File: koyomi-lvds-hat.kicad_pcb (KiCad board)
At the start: 2 copper layers, 65 x 56.5 mm, 27 parts, among them IC1 SN75LVDS83B, J1 RPi_GPIO, J2 20374-R30E-31, J3 aux_sig, J4 qwiic, J5 Conn_01x06, J6 Conn_01x06, J7 Conn_01x06, J8 i2c, U1 AP2114H-2.5

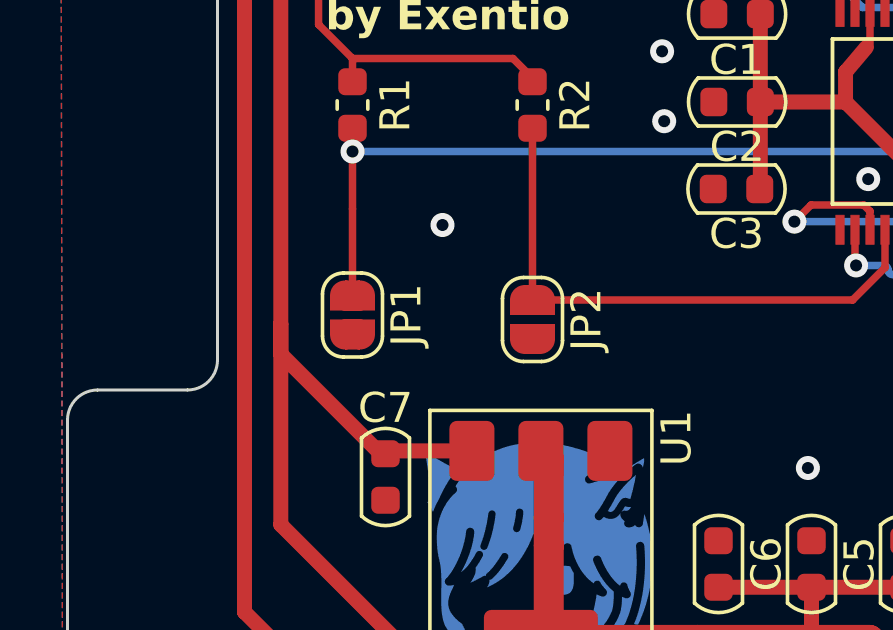
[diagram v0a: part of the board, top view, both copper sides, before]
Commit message: Added 3D models, labels fix
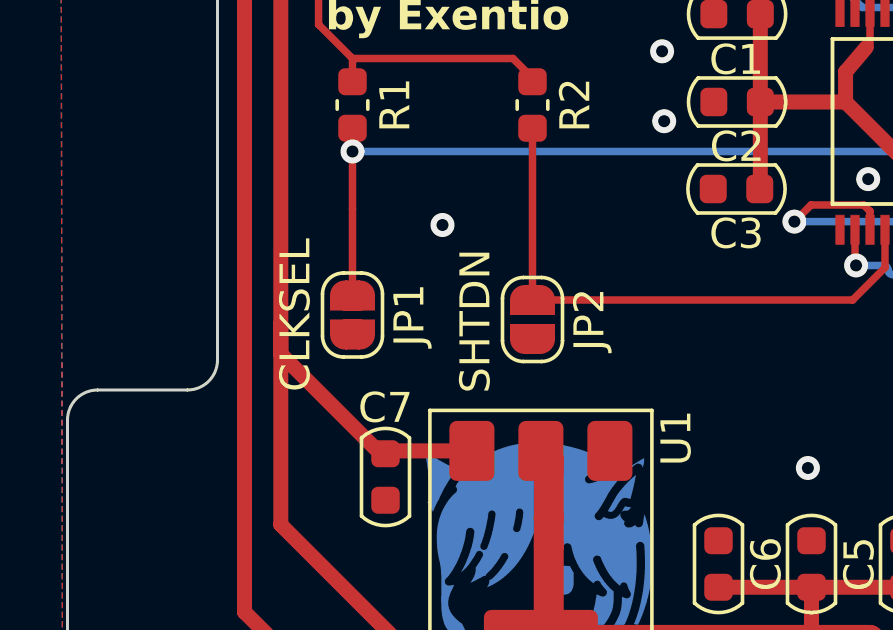
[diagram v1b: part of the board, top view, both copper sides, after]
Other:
- board text added: "CLKSEL"
- board text added: "SHTDN"
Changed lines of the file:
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@@
 		(tags "solder jumper open")
 		(property "Reference" "JP1"
-			(at 0 -1.8 90)
+			(at 0 -1.9 90)
 			(layer "F.SilkS")
 			(effects
@@
 			(at 0 1.9 90)
 			(layer "F.Fab")
+			(hide yes)
 			(effects
 				(font
@@
 			(pintype "passive")
 		)
+		(model "${KIPRJMOD}/lib/20374-R30E-31/20374-R30E-31.step"
+			(offset
+				(xyz 0 0 0)
+			)
+			(scale
+				(xyz 1 1 1)
+			)
+			(rotate
+				(xyz -90 0 180)
+			)
+		)
 	)
 	(footprint "Connector_PinSocket_2.54mm:PinSocket_1x05_P2.54mm_Vertical"
@@
 			(pintype "bidirectional")
 		)
+		(model "${KIPRJMOD}/lib/RPi_Hat_Template/Samtec_HLE-120-02-XXX-DV-BE-XX-XX.stp"
+			(offset
+				(xyz 0 0 0.1)
+			)
+			(scale
+				(xyz 1 1 1)
+			)
+			(rotate
+				(xyz -90 0 90)
+			)
+		)
 	)
 	(footprint "Connector_PinSocket_2.54mm:PinSocket_1x06_P2.54mm_Vertical"
@@
 		)
 		(property "Value" "SN75LVDS83B"
-			(at 0 0 0)
+			(at 0 0 180)
 			(layer "F.Fab")
 			(effects
@@
 		)
 		(property "Description" "\n5/0 Driver LVDS 56-BGA MICROSTAR JUNIOR (7.0x4.5)\n"
-			(at 123.5 50 0)
+			(at 123.5 50 180)
 			(layer "F.Fab")
 			(hide yes)
@@
 		)
 		(property "Availability" "Not in stock"
-			(at 0 0 0)
+			(at 0 0 180)
 			(layer "F.Fab")
 			(hide yes)
@@
 		)
 		(property "Check_prices" "https://www.snapeda.com/parts/SN75LVDS83B/Texas+Instruments/view-part/?ref=eda"
-			(at 0 0 0)
+			(at 0 0 180)
 			(layer "F.Fab")
 			(hide yes)
@@
 		)
 		(property "DIGIKEY" "296-24529-6-ND"
-			(at 0 0 0)
+			(at 0 0 180)
 			(layer "F.Fab")
 			(hide yes)
@@
 		)
 		(property "MF" "Texas Instruments"
-			(at 0 0 0)
+			(at 0 0 180)
 			(layer "F.Fab")
 			(hide yes)
@@
 		)
 		(property "MP" "SN75LVDS83B"
-			(at 0 0 0)
+			(at 0 0 180)
 			(layer "F.Fab")
 			(hide yes)
@@
 		)
 		(property "Package" "TFSOP-56 Texas Instruments"
-			(at 0 0 0)
+			(at 0 0 180)
 			(layer "F.Fab")
 			(hide yes)
@@
 		)
 		(property "Price" "None"
-			(at 0 0 0)
+			(at 0 0 180)
 			(layer "F.Fab")
 			(hide yes)
@@
 		)
 		(property "SnapEDA_Link" "https://www.snapeda.com/parts/SN75LVDS83B/Texas+Instruments/view-part/?ref=snap"
-			(at 0 0 0)
+			(at 0 0 180)
 			(layer "F.Fab")
 			(hide yes)
@@
 			(pintype "bidirectional")
 		)
+		(model "${KIPRJMOD}/lib/SN75LVDS83B/SN75LVDS83B.step"
+			(offset
+				(xyz 0 0 0)
+			)
+			(scale
+				(xyz 1 1 1)
+			)
+			(rotate
+				(xyz -90 0 90)
+			)
+		)
 	)
 	(footprint "Connector_PinHeader_2.54mm:PinHeader_1x06_P2.54mm_Vertical"
@@
 		(tags "solder jumper open")
 		(property "Reference" "JP2"
-			(at 0 -1.8 90)
+			(at 0 -1.9 90)
 			(layer "F.SilkS")
 			(effects
@@
 			(at 0 1.9 90)
 			(layer "F.Fab")
+			(hide yes)
 			(effects
 				(font
@@
 			(pintype "passive")
 		)
-		(model "${KICAD6_3DMODEL_DIR}/Connector_JST.3dshapes/JST_SH_SM04B-SRSS-TB_1x04-1MP_P1.00mm_Horizontal.wrl"
+		(model "${KIPRJMOD}/lib/JST_SH_SM04B-SRSS-TB_1x04-1MP_P1.00mm_Horizontal.STEP"
 			(offset
-				(xyz 0 0 0)
+				(xyz 0 1.35 -0.3)
 			)
 			(scale
@@
 			)
 			(rotate
-				(xyz 0 0 0)
+				(xyz -90 0 0)
 			)
 		)
@@
 		)
 	)
+	(gr_text "SHTDN"
+		(at 104.6 56.7 90)
+		(layer "F.SilkS")
+		(effects
+			(font
+				(size 1 1)
+				(thickness 0.15)
+			)
+		)
+	)
+	(gr_text "CLKSEL"
+		(at 98.6 56.5 90)
+		(layer "F.SilkS")
+		(effects
+			(font
+				(size 1 1)
+				(thickness 0.15)
+			)
+		)
+	)

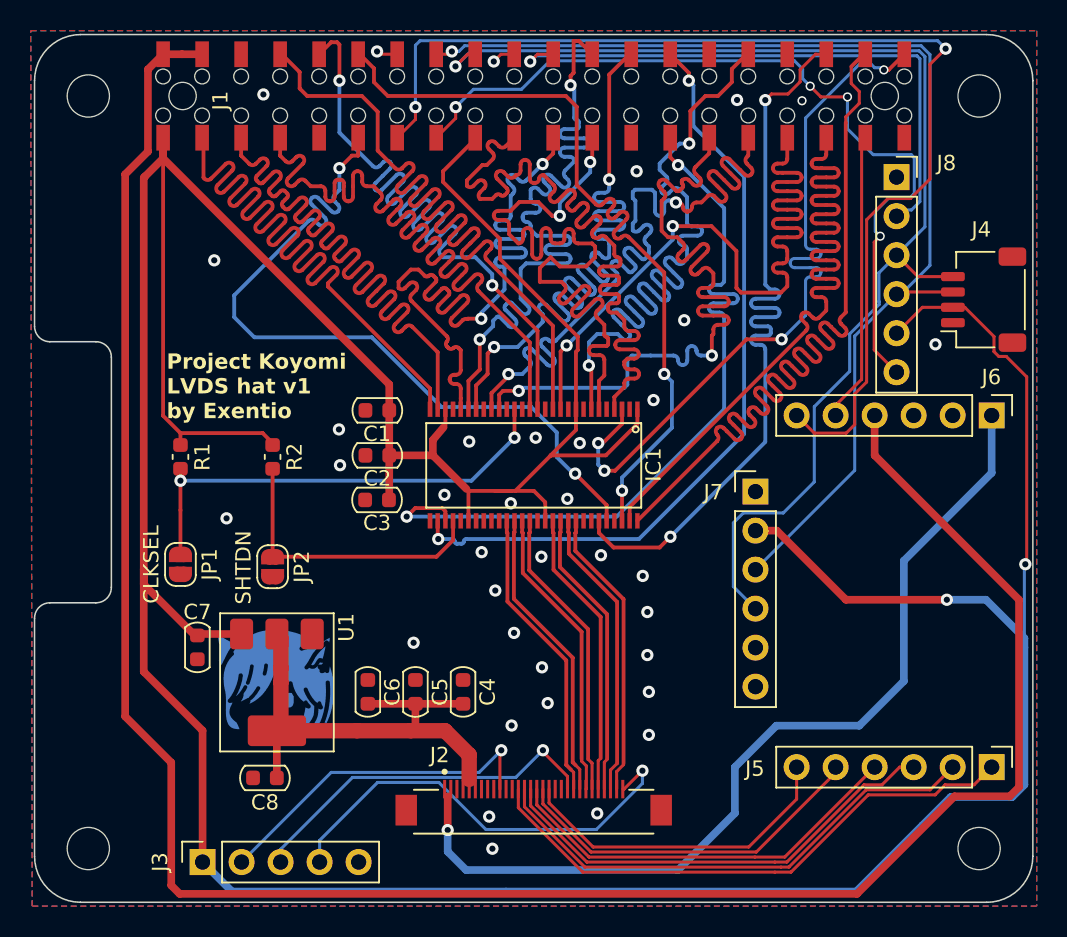
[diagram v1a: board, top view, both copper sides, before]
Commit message: v1.1 - fixed hat connector side, added series resistors
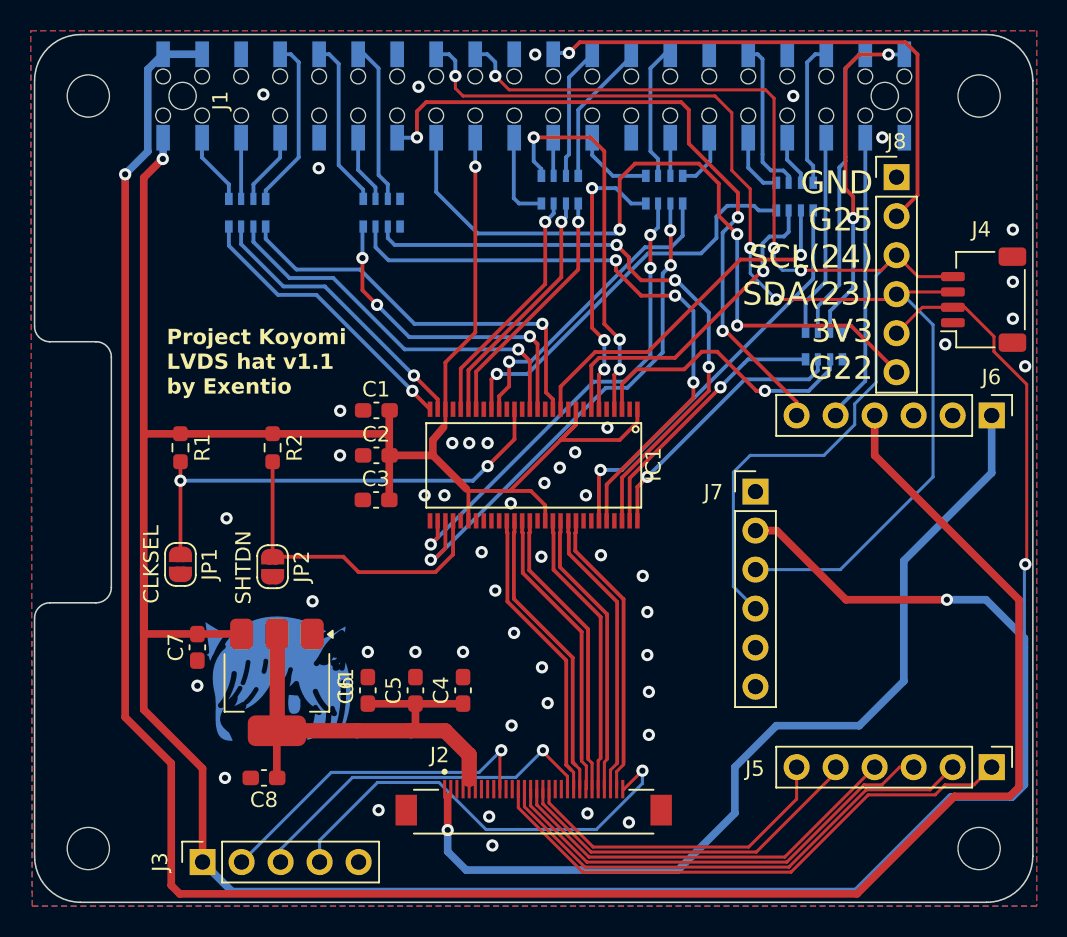
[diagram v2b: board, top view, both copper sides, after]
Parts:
- added RN1: 47, Resistor_SMD:R_Array_Convex_4x0603, B.Cu at (104.8, 33.6)
- added RN2: 47, Resistor_SMD:R_Array_Convex_4x0603, B.Cu at (113.6, 33.6)
- added RN3: 47, Resistor_SMD:R_Array_Convex_4x0603, B.Cu at (125.2, 32.1)
- added RN4: 47, Resistor_SMD:R_Array_Convex_4x0603, B.Cu at (132.0, 32.1)
- added RN5: 47, Resistor_SMD:R_Array_Convex_4x0603, B.Cu at (140.5, 32.5)
- added RN6: 47, Resistor_SMD:R_Array_Convex_4x0603, B.Cu at (142.4, 42.2)
- C1, C2, C3, C4, C5, C6, C7, C8: footprint PCM_Capacitor_SMD_US_Handsoldering_AKL:C_0603_1608Metric -> Capacitor_SMD:C_0603_1608Metric_Pad1.08x0.95mm_HandSolder
- J8: footprint Connector_PinSocket_2.54mm:PinSocket_1x06_P2.54mm_Vertical -> Connector_PinHeader_2.54mm:PinHeader_1x06_P2.54mm_Vertical
- R1, R2: footprint Capacitor_SMD:C_0603_1608Metric -> Resistor_SMD:R_0603_1608Metric_Pad0.98x0.95mm_HandSolder
- REF**: footprint exentio_pcb_art:blob -> exentio_art:exentio_blob
- U1: footprint PCM_Package_TO_SOT_SMD_AKL:SOT-223-3_TabPin2 -> Package_TO_SOT_SMD:SOT-223-3_TabPin2
- moved R1 0.60 mm to (100.5, 48.9)
- moved R2 0.60 mm to (106.5, 48.9)
- moved C4 0.10 mm to (118.9, 64.7)
- moved C5 0.10 mm to (115.8, 64.7)
- moved C6 0.10 mm to (112.7, 64.7)
- moved C1 0.06 mm to (113.3, 46.5)
- moved C2 0.06 mm to (113.3, 49.4)
- moved C3 0.06 mm to (113.2, 52.3)
- moved C8 0.06 mm to (105.9, 70.4)
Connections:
- IC1 pad 11: G3 -> D12
- IC1 pad 12: G4 -> D13
- IC1 pad 14: G5 -> D14
- IC1 pad 15: B0 -> D15
- IC1 pad 19: B1 -> D18
- IC1 pad 20: B2 -> D19
- IC1 pad 22: B3 -> D20
- IC1 pad 23: B4 -> D21
- IC1 pad 24: B5 -> D22
- IC1 pad 27: HSYNC -> D24
- IC1 pad 28: VSYNC -> D25
- IC1 pad 3: R5 -> D6
- IC1 pad 30: ENABLE -> D26
- IC1 pad 31: CLKIN -> L_CLKIN
- IC1 pad 4: G0 -> D7
- IC1 pad 51: R0 -> D0
- IC1 pad 52: R1 -> D1
- IC1 pad 54: R2 -> D2
- IC1 pad 55: R3 -> D3
- IC1 pad 56: R4 -> D4
- IC1 pad 6: G1 -> D8
- IC1 pad 7: G2 -> D9
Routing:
- net HSYNC: track 53.6 -> 4.23 mm
- net VSYNC: track 53.7 -> 4.70 mm
- net B0: track 53.6 -> 4.70 mm
- net CLKIN: track 50.9 -> 2.49 mm, vias 2 -> 0
- net B5: track 50.5 -> 2.49 mm, vias 2 -> 0
- net G0: track 53.5 -> 5.89 mm
- net G3: track 50.7 -> 3.29 mm, vias 2 -> 0
- net B1: track 50.6 -> 3.75 mm, vias 2 -> 0
- net R1: track 50.9 -> 4.45 mm, vias 2 -> 0
- net B2: track 50.5 -> 4.19 mm, vias 2 -> 0
- net G1: track 50.6 -> 5.19 mm, vias 2 -> 0
- net G4: track 53.8 -> 11.2 mm
- net ENABLE: track 51.0 -> 8.88 mm, vias 2 -> 0
- net B4: track 50.6 -> 8.63 mm, vias 2 -> 0
- net R0: track 50.9 -> 9.47 mm, vias 2 -> 0
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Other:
- board text added: "Project Koyomi LVDS hat v1.1 by Exentio"
- board text removed: "Project Koyomi LVDS hat v1 by Exentio"

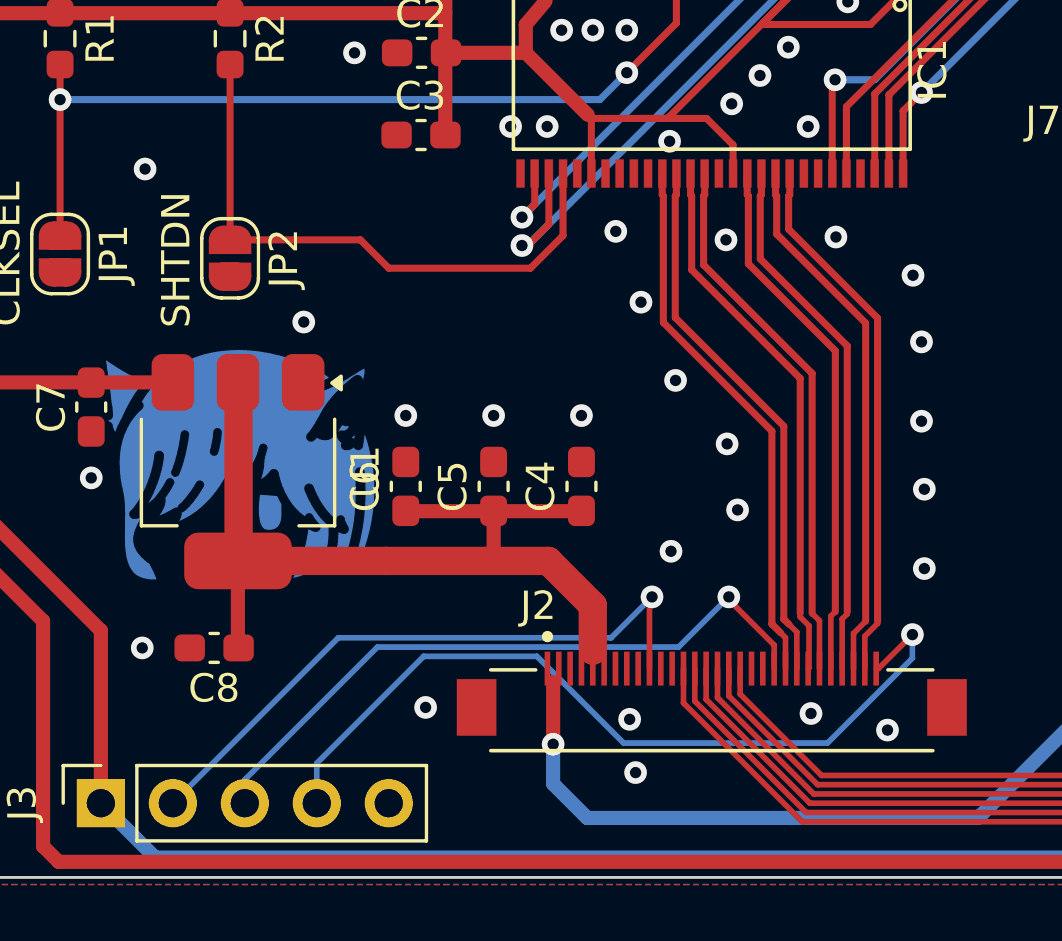
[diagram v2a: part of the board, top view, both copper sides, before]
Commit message: Added LVDS common mode filters
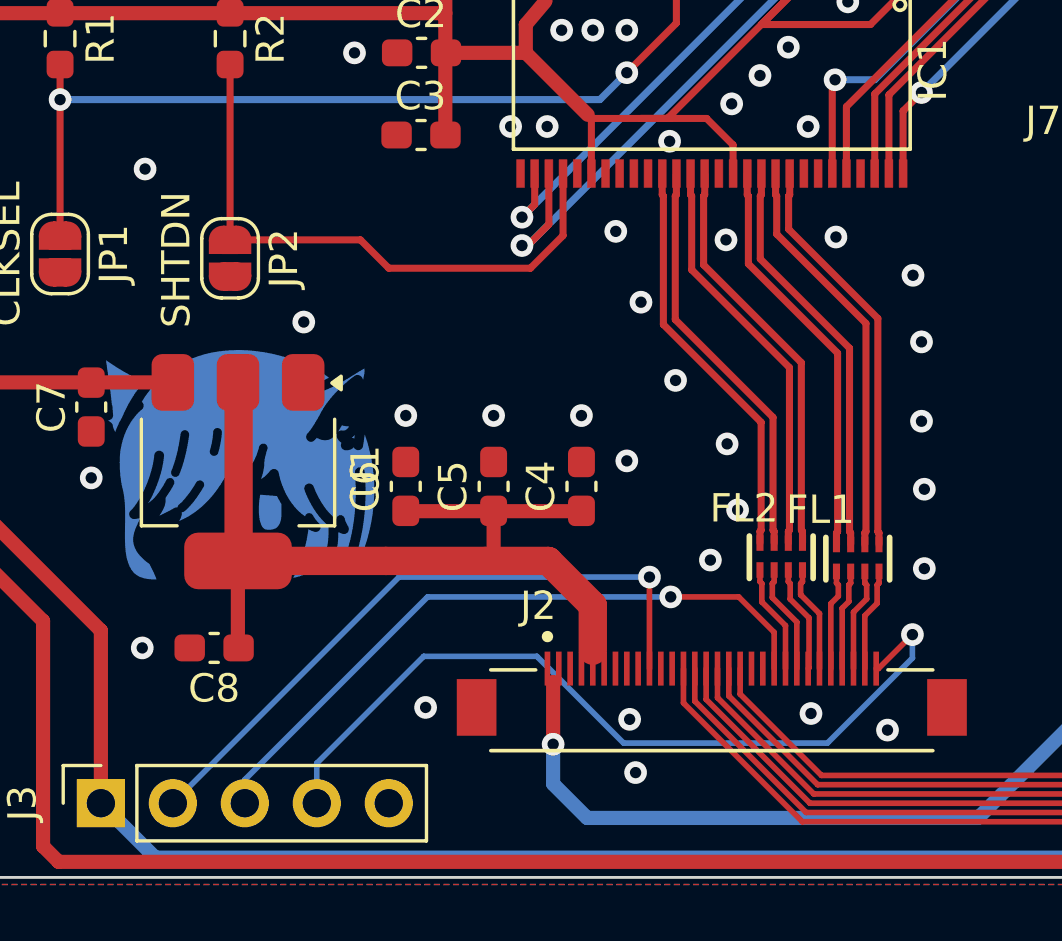
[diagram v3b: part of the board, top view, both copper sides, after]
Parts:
- added FL1: DLP2ADN121HL4L, Murata_DLP2ADN121HL4L:Murata_DLP2ADN121HL4L, F.Cu at (128.6, 67.2)
- added FL2: DLP2ADN121HL4L, Murata_DLP2ADN121HL4L:Murata_DLP2ADN121HL4L, F.Cu at (125.9, 67.2)
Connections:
- IC1 pad 39: RXCLK+ -> Net-(IC1-CLCKOUTP)
- IC1 pad 40: RXCLK- -> Net-(IC1-CLCKOUTM)
- IC1 pad 41: RX2+ -> Net-(IC1-Y2P)
- IC1 pad 42: RX2- -> Net-(IC1-Y2M)
- IC1 pad 45: RX1+ -> Net-(IC1-Y1P)
- IC1 pad 46: RX1- -> Net-(IC1-Y1M)
- IC1 pad 47: RX0+ -> Net-(IC1-Y0P)
- IC1 pad 48: RX0- -> Net-(IC1-Y0M)
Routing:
- net RXCLK+: track 19.3 -> 3.85 mm
- net RX2+: track 19.2 -> 3.79 mm
- net RX2-: track 19.2 -> 3.78 mm
- net RXCLK-: track 19.3 -> 3.87 mm
- net RX0-: track 19.0 -> 3.64 mm
- net RX0+: track 19.0 -> 3.65 mm
- net RX1-: track 18.8 -> 3.55 mm
- net RX1+: track 18.8 -> 3.57 mm
- net Net-(IC1-CLCKOUTM): track 0.00 -> 14.5 mm
- net Net-(IC1-Y2P): track 0.00 -> 14.5 mm
- net Net-(IC1-Y2M): track 0.00 -> 14.5 mm
- net Net-(IC1-CLCKOUTP): track 0.00 -> 14.5 mm
- net Net-(IC1-Y1M): track 0.00 -> 14.4 mm
- net Net-(IC1-Y0M): track 0.00 -> 14.4 mm
- net Net-(IC1-Y1P): track 0.00 -> 14.4 mm
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
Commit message: Gerbers and JLCPCB files update
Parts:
- C2, C5: value 0.1uF -> 100nF
- C3, C6: value 0.01uF -> 10nF
